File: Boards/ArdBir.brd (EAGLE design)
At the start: 64 x 38.6 mm, 30 parts, among them IC2 LM2940

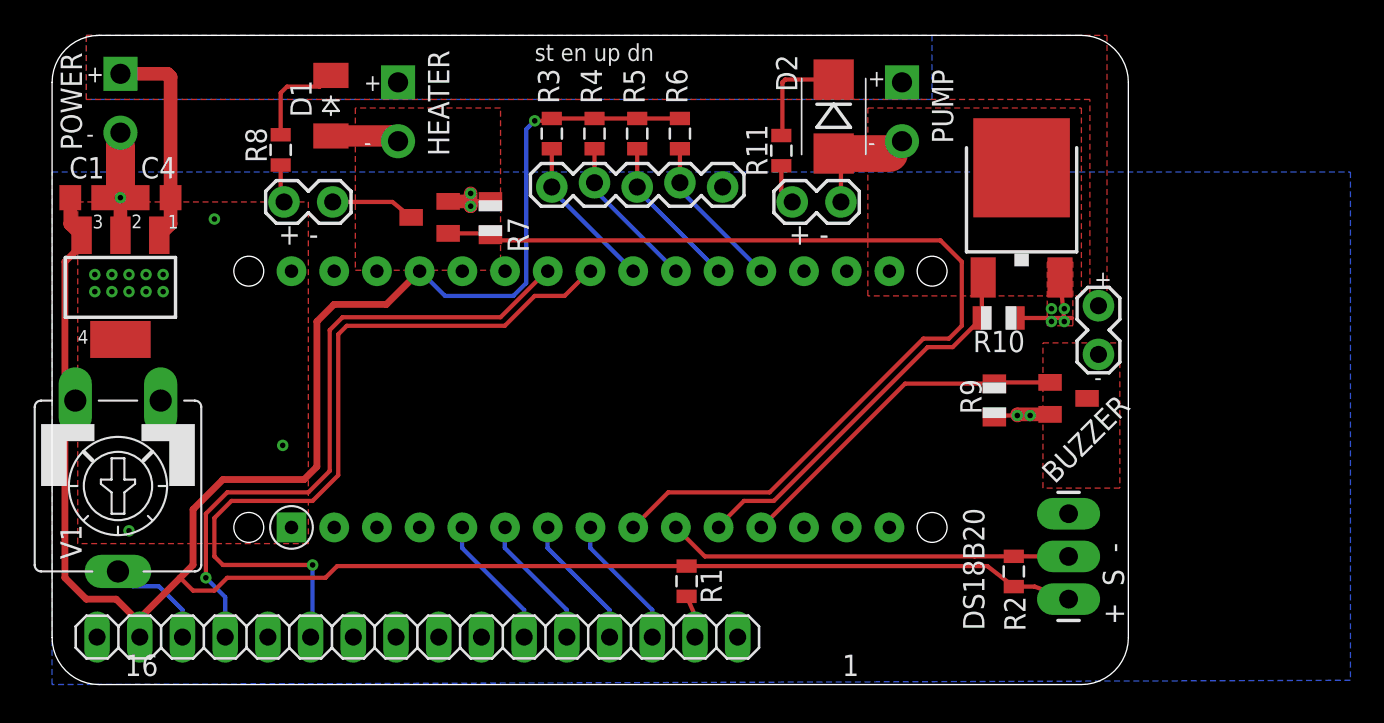
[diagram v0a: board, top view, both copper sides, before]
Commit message: Added part numbers for MOSFETs
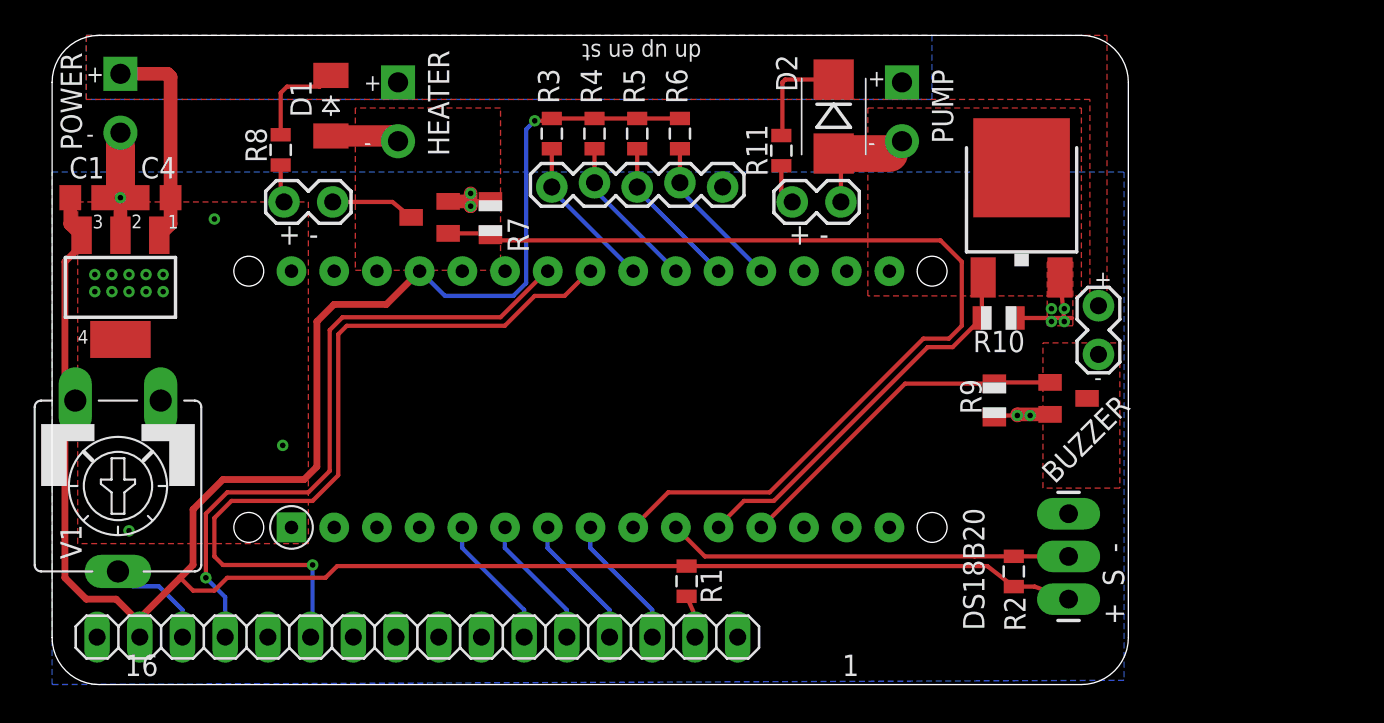
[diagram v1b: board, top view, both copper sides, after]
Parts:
- BUZZER_MOSFET: value buzzer -> SI2302CDS-T1-E3
- HEATER_MOSFET: value heater -> SI2302CDS-T1-E3
- IC2: value LM2940 -> LM2940IMP-5.0/NOPB
- PUMP_MOSFET: value GOVPRESS -> BUK9275-100A
- renumbered U$2 to HEATER_MOSFET, U$3 to BUZZER_MOSFET, U$4 to PUMP_MOSFET
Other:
- board text added: "dn up en st"
- board text removed: "st en up dn"
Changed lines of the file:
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@@
 <text x="43.815" y="26.162" size="1.27" layer="121" font="vector" ratio="5">+ -</text>
 <text x="13.462" y="26.162" size="1.27" layer="121" font="vector" ratio="5">+ -</text>
-<text x="28.702" y="37.084" size="1.016" layer="121" font="vector" ratio="7">st en up dn</text>
+<text x="38.608" y="38.1" size="1.016" layer="121" font="vector" ratio="7" rot="SR180">dn up en st</text>
 <text x="61.976" y="23.622" size="1.016" layer="121" font="vector" ratio="7">+</text>
 <text x="61.976" y="17.78" size="1.016" layer="121" font="vector" ratio="7">-</text>
@@
 </element>
 <element name="U$1" library="jet-lib" package="PDIP-32" value="ARDUINONANO" x="11.6967" y="9.344659375" smashed="yes" rot="R90"/>
-<element name="U$2" library="SparkFun" package="SOT23" value="heater" x="22.4536" y="27.78251875" smashed="yes" rot="R90"/>
+<element name="HEATER_MOSFET" library="SparkFun" package="SOT23" value="SI2302CDS-T1-E3" x="22.4536" y="27.78251875" smashed="yes" rot="R90"/>
 <element name="R7" library="adafruit" package="R0805" value="10k" x="26.06801875" y="27.739340625" smashed="yes" rot="R90">
 <attribute name="NAME" x="28.35401875" y="25.707340625" size="1.27" layer="25" font="vector" ratio="5" rot="R90"/>
@@
 <attribute name="VALUE" x="41.148" y="32.893" size="1.27" layer="27" rot="R180"/>
 </element>
-<element name="U$3" library="SparkFun" package="SOT23" value="buzzer" x="60.452" y="17.018" smashed="yes" rot="R270"/>
+<element name="BUZZER_MOSFET" library="SparkFun" package="SOT23" value="SI2302CDS-T1-E3" x="60.452" y="17.018" smashed="yes" rot="R270"/>
 <element name="HEATER_LED" library="SparkFun" package="1X02_LOCK" value="" x="16.51" y="28.702" smashed="yes" rot="R180">
 <attribute name="VALUE" x="17.78" y="31.877" size="1.27" layer="27" rot="R180"/>
@@
 <attribute name="NAME" x="7.366" y="31.369" size="1.27" layer="25" font="vector" ratio="5" rot="R180"/>
 </element>
-<element name="IC2" library="national-semiconductor" package="SOT223" value="LM2940" x="4.064" y="23.622" smashed="yes" rot="R180">
+<element name="IC2" library="national-semiconductor" package="SOT223" value="LM2940IMP-5.0/NOPB" x="4.064" y="23.622" smashed="yes" rot="R180">
 <attribute name="OC_FARNELL" value="1469063" x="19.304" y="20.32" size="1.778" layer="27" rot="R180" display="off"/>
 <attribute name="OC_NEWARK" value="41K4524" x="19.304" y="20.32" size="1.778" layer="27" rot="R180" display="off"/>
@@
 <attribute name="NAME" x="1.016" y="30.099" size="1.27" layer="25" font="vector" ratio="5"/>
 </element>
-<element name="U$4" library="dpak" package="DPAK" value="GOVPRESS" x="57.658" y="30.734" smashed="yes"/>
+<element name="PUMP_MOSFET" library="dpak" package="DPAK" value="BUK9275-100A" x="57.658" y="30.734" smashed="yes"/>
 </elements>
 <signals>
@@
 <contactref element="R9" pad="2"/>
 <contactref element="R7" pad="2"/>
-<contactref element="U$2" pad="2"/>
+<contactref element="HEATER_MOSFET" pad="2"/>
 <polygon width="0.4064" layer="16" isolate="0.3048" rank="6">
 <vertex x="0" y="30.48"/>
-<vertex x="77.216" y="30.48"/>
-<vertex x="77.216" y="0.254"/>
+<vertex x="63.754" y="30.48"/>
+<vertex x="63.754" y="0.254"/>
 <vertex x="0" y="0"/>
 </polygon>
-<contactref element="U$3" pad="2"/>
+<contactref element="BUZZER_MOSFET" pad="2"/>
 <contactref element="DS18B20" pad="3"/>
 <contactref element="BUTTONS" pad="1"/>
@@
 <contactref element="C1" pad="2"/>
 <via x="4.064" y="28.956" extent="1-16" drill="0.3302" shape="square"/>
-<contactref element="U$4" pad="3"/>
+<contactref element="PUMP_MOSFET" pad="3"/>
 <via x="24.892" y="28.448" extent="1-16" drill="0.3302" shape="square"/>
 <via x="59.436" y="22.352" extent="1-16" drill="0.3302" shape="square"/>
@@
 <signal name="D8">
 <contactref element="R10" pad="1"/>
-<contactref element="U$4" pad="1"/>
+<contactref element="PUMP_MOSFET" pad="1"/>
 <contactref element="U$1" pad="D8"/>
 <wire x1="55.373" y1="24.209" x2="55.29401875" y2="24.03398125" width="0.254" layer="1"/>
@@
 <signal name="D9">
 <contactref element="R9" pad="1"/>
-<contactref element="U$3" pad="1"/>
+<contactref element="BUZZER_MOSFET" pad="1"/>
 <contactref element="U$1" pad="D9"/>
 <wire x1="42.1767" y1="9.344659375" x2="50.728121875" y2="17.89608125" width="0.254" layer="1"/>
@@
 <signal name="HEATER_OUT">
 <contactref element="D1" pad="A"/>
-<contactref element="U$2" pad="3"/>
+<contactref element="HEATER_MOSFET" pad="3"/>
 <contactref element="HEATER_LED" pad="1"/>
 <contactref element="HEATER" pad="2"/>
@@
 </signal>
 <signal name="BUZZER_OUT">
-<contactref element="U$3" pad="3"/>
+<contactref element="BUZZER_MOSFET" pad="3"/>
 <contactref element="BUZZER" pad="2"/>
 <polygon width="0.254" layer="1" isolate="0.254" thermals="no">
@@
 <contactref element="PUMP_LED" pad="1"/>
 <contactref element="PUMP" pad="2"/>
-<contactref element="U$4" pad="4"/>
+<contactref element="PUMP_MOSFET" pad="4"/>
 <wire x1="50.546" y1="32.314" x2="49.814" y2="31.582" width="1.27" layer="1"/>
 <wire x1="49.814" y1="31.582" x2="46.482" y2="31.582" width="2.1844" layer="1"/>
@@
 <signal name="D6">
 <contactref element="R7" pad="1"/>
-<contactref element="U$2" pad="1"/>
+<contactref element="HEATER_MOSFET" pad="1"/>
 <contactref element="U$1" pad="D6"/>
 <wire x1="34.5567" y1="9.344659375" x2="36.642040625" y2="11.43" width="0.254" layer="1"/>
